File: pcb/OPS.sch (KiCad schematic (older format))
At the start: 36 parts, among them Q13 Q_PNP_EBC, Q14 Q_NPN_ECB, Q15 Q_PNP_EBC, Q16 Q_NPN_ECB, Q17 Q_NPN_ECB, Q18 Q_PNP_EBC, Q19 Q_NPN_ECB, Q20 Q_PNP_EBC, Q21 Q_NPN_ECB, Q22 Q_PNP_EBC, Q23 Q_NPN_ECB, Q24 Q_NPN_ECB, Q25 Q_PNP_EBC, Q26 Q_PNP_EBC

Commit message: Problema sobre power conections arreglado, ahora hay otros quilombos, creo que tiene que ver con el encapsulado de los transistores.
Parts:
- C5, C6: footprint Capacitors_SMD:C_0201 -> Capacitors_SMD:C_0603_HandSoldering
- Q13, Q14, Q15, Q16, Q17, Q18, Q19, Q20, Q21, Q22: footprint Transistors_TO-220:TO-220_Bipolar-BCE_Horizontal -> Transistors_TO-220:TO-220_Bipolar-BCE_Vertical_LargePads
- R15, R16, R17, R18, R19, R20, R21, R22, R23, R24, R25, R26, R27: footprint Resistors_SMD:R_0201 -> Resistors_SMD:R_0603_HandSoldering
- R28: footprint Resistors_SMD:R_0201 -> Resistors_SMD:R_0805_HandSoldering
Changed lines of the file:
@@
 F 0 "Q13" H 3600 1400 50  0000 R CNN
 F 1 "Q_PNP_EBC" H 3900 1300 50  0000 R CNN
-F 2 "Transistors_TO-220:TO-220_Bipolar-BCE_Horizontal" H 3500 1450 29  0001 C CNN
+F 2 "Transistors_TO-220:TO-220_Bipolar-BCE_Vertical_LargePads" H 3500 1450 29  0001 C CNN
 F 3 "" H 3300 1350 60  0000 C CNN
 	1    3300 1350
@@
 F 0 "Q15" H 4200 1400 50  0000 R CNN
 F 1 "Q_PNP_EBC" H 4500 1300 50  0000 R CNN
-F 2 "Transistors_TO-220:TO-220_Bipolar-BCE_Horizontal" H 4100 1450 29  0001 C CNN
+F 2 "Transistors_TO-220:TO-220_Bipolar-BCE_Vertical_LargePads" H 4100 1450 29  0001 C CNN
 F 3 "" H 3900 1350 60  0000 C CNN
 	1    3900 1350
@@
 F 0 "R15" V 3280 1900 50  0000 C CNN
 F 1 "R" V 3200 1900 50  0000 C CNN
-F 2 "Resistors_SMD:R_0201" V 3130 1900 30  0001 C CNN
+F 2 "Resistors_SMD:R_0603_HandSoldering" V 3130 1900 30  0001 C CNN
 F 3 "" H 3200 1900 30  0000 C CNN
 	1    3200 1900
@@
 F 0 "R17" V 4380 2550 50  0000 C CNN
 F 1 "R" V 4300 2550 50  0000 C CNN
-F 2 "Resistors_SMD:R_0201" V 4230 2550 30  0001 C CNN
+F 2 "Resistors_SMD:R_0603_HandSoldering" V 4230 2550 30  0001 C CNN
 F 3 "" H 4300 2550 30  0000 C CNN
 	1    4300 2550
@@
 F 0 "Q21" H 5550 1900 50  0000 R CNN
 F 1 "Q_NPN_ECB" H 5850 1800 50  0000 R CNN
-F 2 "Transistors_TO-220:TO-220_Bipolar-BCE_Horizontal" H 5450 1950 29  0001 C CNN
+F 2 "Transistors_TO-220:TO-220_Bipolar-BCE_Vertical_LargePads" H 5450 1950 29  0001 C CNN
 F 3 "" H 5250 1850 60  0000 C CNN
 	1    5250 1850
@@
 F 0 "R24" V 5430 2200 50  0000 C CNN
 F 1 "R" V 5350 2200 50  0000 C CNN
-F 2 "Resistors_SMD:R_0201" V 5280 2200 30  0001 C CNN
+F 2 "Resistors_SMD:R_0603_HandSoldering" V 5280 2200 30  0001 C CNN
 F 3 "" H 5350 2200 30  0000 C CNN
 	1    5350 2200
@@
 F 0 "Q17" H 4400 3250 50  0000 R CNN
 F 1 "Q_NPN_ECB" H 4700 3150 50  0000 R CNN
-F 2 "Transistors_TO-220:TO-220_Bipolar-BCE_Horizontal" H 4300 3300 29  0001 C CNN
+F 2 "Transistors_TO-220:TO-220_Bipolar-BCE_Vertical_LargePads" H 4300 3300 29  0001 C CNN
 F 3 "" H 4100 3200 60  0000 C CNN
 	1    4100 3200
@@
 F 0 "R19" V 4530 3000 50  0000 C CNN
 F 1 "R" V 4450 3000 50  0000 C CNN
-F 2 "Resistors_SMD:R_0201" V 4380 3000 30  0001 C CNN
+F 2 "Resistors_SMD:R_0603_HandSoldering" V 4380 3000 30  0001 C CNN
 F 3 "" H 4450 3000 30  0000 C CNN
 	1    4450 3000
@@
 F 0 "C5" H 3675 3000 50  0000 L CNN
 F 1 "C" H 3675 2800 50  0000 L CNN
-F 2 "Capacitors_SMD:C_0201" H 3688 2750 30  0001 C CNN
+F 2 "Capacitors_SMD:C_0603_HandSoldering" H 3688 2750 30  0001 C CNN
 F 3 "" H 3650 2900 60  0000 C CNN
 	1    3650 2900
@@
 F 0 "Q19" H 5150 2600 50  0000 R CNN
 F 1 "Q_NPN_ECB" H 5450 2500 50  0000 R CNN
-F 2 "Transistors_TO-220:TO-220_Bipolar-BCE_Horizontal" H 5050 2650 29  0001 C CNN
+F 2 "Transistors_TO-220:TO-220_Bipolar-BCE_Vertical_LargePads" H 5050 2650 29  0001 C CNN
 F 3 "" H 4850 2550 60  0000 C CNN
 	1    4850 2550
@@
 F 0 "R20" V 4530 3550 50  0000 C CNN
 F 1 "R" V 4450 3550 50  0000 C CNN
-F 2 "Resistors_SMD:R_0201" V 4380 3550 30  0001 C CNN
+F 2 "Resistors_SMD:R_0603_HandSoldering" V 4380 3550 30  0001 C CNN
 F 3 "" H 4450 3550 30  0000 C CNN
 	1    4450 3550
@@
 F 0 "R22" V 5030 3250 50  0000 C CNN
 F 1 "R" V 4950 3250 50  0000 C CNN
-F 2 "Resistors_SMD:R_0201" V 4880 3250 30  0001 C CNN
+F 2 "Resistors_SMD:R_0603_HandSoldering" V 4880 3250 30  0001 C CNN
 F 3 "" H 4950 3250 30  0000 C CNN
 	1    4950 3250
@@
 F 0 "R26" V 6030 3300 50  0000 C CNN
 F 1 "R" V 5950 3300 50  0000 C CNN
-F 2 "Resistors_SMD:R_0201" V 5880 3300 30  0001 C CNN
+F 2 "Resistors_SMD:R_0603_HandSoldering" V 5880 3300 30  0001 C CNN
 F 3 "" H 5950 3300 30  0000 C CNN
 	1    5950 3300
@@
 F 0 "R16" V 3280 5200 50  0000 C CNN
 F 1 "R" V 3200 5200 50  0000 C CNN
-F 2 "Resistors_SMD:R_0201" V 3130 5200 30  0001 C CNN
+F 2 "Resistors_SMD:R_0603_HandSoldering" V 3130 5200 30  0001 C CNN
 F 3 "" H 3200 5200 30  0000 C CNN
 	1    3200 5200
@@
 F 0 "R18" V 4380 4550 50  0000 C CNN
 F 1 "R" V 4300 4550 50  0000 C CNN
-F 2 "Resistors_SMD:R_0201" V 4230 4550 30  0001 C CNN
+F 2 "Resistors_SMD:R_0603_HandSoldering" V 4230 4550 30  0001 C CNN
 F 3 "" H 4300 4550 30  0000 C CNN
 	1    4300 4550
@@
 F 0 "R25" V 5430 4900 50  0000 C CNN
 F 1 "R" V 5350 4900 50  0000 C CNN
-F 2 "Resistors_SMD:R_0201" V 5280 4900 30  0001 C CNN
+F 2 "Resistors_SMD:R_0603_HandSoldering" V 5280 4900 30  0001 C CNN
 F 3 "" H 5350 4900 30  0000 C CNN
 	1    5350 4900
@@
 F 0 "R21" V 4530 4100 50  0000 C CNN
 F 1 "R" V 4450 4100 50  0000 C CNN
-F 2 "Resistors_SMD:R_0201" V 4380 4100 30  0001 C CNN
+F 2 "Resistors_SMD:R_0603_HandSoldering" V 4380 4100 30  0001 C CNN
 F 3 "" H 4450 4100 30  0000 C CNN
 	1    4450 4100
@@
 F 0 "C6" H 3675 4300 50  0000 L CNN
 F 1 "C" H 3675 4100 50  0000 L CNN
-F 2 "Capacitors_SMD:C_0201" H 3688 4050 30  0001 C CNN
+F 2 "Capacitors_SMD:C_0603_HandSoldering" H 3688 4050 30  0001 C CNN
 F 3 "" H 3650 4200 60  0000 C CNN
 	1    3650 4200
@@
 F 0 "R23" V 5030 3850 50  0000 C CNN
 F 1 "R" V 4950 3850 50  0000 C CNN
-F 2 "Resistors_SMD:R_0201" V 4880 3850 30  0001 C CNN
+F 2 "Resistors_SMD:R_0603_HandSoldering" V 4880 3850 30  0001 C CNN
 F 3 "" H 4950 3850 30  0000 C CNN
 	1    4950 3850
@@
 F 0 "R27" V 6030 3800 50  0000 C CNN
 F 1 "R" V 5950 3800 50  0000 C CNN
-F 2 "Resistors_SMD:R_0201" V 5880 3800 30  0001 C CNN
+F 2 "Resistors_SMD:R_0603_HandSoldering" V 5880 3800 30  0001 C CNN
 F 3 "" H 5950 3800 30  0000 C CNN
 	1    5950 3800
@@
 F 0 "Q14" H 3600 5800 50  0000 R CNN
 F 1 "Q_NPN_ECB" H 3900 5700 50  0000 R CNN
-F 2 "Transistors_TO-220:TO-220_Bipolar-BCE_Horizontal" H 3500 5850 29  0001 C CNN
+F 2 "Transistors_TO-220:TO-220_Bipolar-BCE_Vertical_LargePads" H 3500 5850 29  0001 C CNN
 F 3 "" H 3300 5750 60  0000 C CNN
 	1    3300 5750
@@
 F 0 "Q18" H 4400 3950 50  0000 R CNN
 F 1 "Q_PNP_EBC" H 4700 3850 50  0000 R CNN
-F 2 "Transistors_TO-220:TO-220_Bipolar-BCE_Horizontal" H 4300 4000 29  0001 C CNN
+F 2 "Transistors_TO-220:TO-220_Bipolar-BCE_Vertical_LargePads" H 4300 4000 29  0001 C CNN
 F 3 "" H 4100 3900 60  0000 C CNN
 	1    4100 3900
@@
 F 0 "Q16" H 4200 5800 50  0000 R CNN
 F 1 "Q_NPN_ECB" H 4500 5700 50  0000 R CNN
-F 2 "Transistors_TO-220:TO-220_Bipolar-BCE_Horizontal" H 4100 5850 29  0001 C CNN
+F 2 "Transistors_TO-220:TO-220_Bipolar-BCE_Vertical_LargePads" H 4100 5850 29  0001 C CNN
 F 3 "" H 3900 5750 60  0000 C CNN
 	1    3900 5750
@@
 F 0 "Q20" H 5150 4600 50  0000 R CNN
 F 1 "Q_PNP_EBC" H 5450 4500 50  0000 R CNN
-F 2 "Transistors_TO-220:TO-220_Bipolar-BCE_Horizontal" H 5050 4650 29  0001 C CNN
+F 2 "Transistors_TO-220:TO-220_Bipolar-BCE_Vertical_LargePads" H 5050 4650 29  0001 C CNN
 F 3 "" H 4850 4550 60  0000 C CNN
 	1    4850 4550
@@
 F 0 "Q22" H 5550 5300 50  0000 R CNN
 F 1 "Q_PNP_EBC" H 5850 5200 50  0000 R CNN
-F 2 "Transistors_TO-220:TO-220_Bipolar-BCE_Horizontal" H 5450 5350 29  0001 C CNN
+F 2 "Transistors_TO-220:TO-220_Bipolar-BCE_Vertical_LargePads" H 5450 5350 29  0001 C CNN
 F 3 "" H 5250 5250 60  0000 C CNN
 	1    5250 5250
@@
 F 0 "R28" V 6480 3800 50  0000 C CNN
 F 1 "R" V 6400 3800 50  0000 C CNN
-F 2 "Resistors_SMD:R_0201" V 6330 3800 30  0001 C CNN
+F 2 "Resistors_SMD:R_0805_HandSoldering" V 6330 3800 30  0001 C CNN
 F 3 "" H 6400 3800 30  0000 C CNN
 	1    6400 3800
@@
 	6400 3550 6400 3650
 $Comp
-L GND #PWR017
+L GND #PWR028
 U 1 1 555E69E7
 P 6400 4000
-F 0 "#PWR017" H 6400 3750 50  0001 C CNN
+F 0 "#PWR028" H 6400 3750 50  0001 C CNN
 F 1 "GND" H 6400 3850 50  0000 C CNN
 F 2 "" H 6400 4000 60  0000 C CNN
@@
 	6400 3950 6400 4000
 $Comp
-L GND #PWR018
+L GND #PWR029
 U 1 1 555F209B
 P 3200 5050
-F 0 "#PWR018" H 3200 4800 50  0001 C CNN
+F 0 "#PWR029" H 3200 4800 50  0001 C CNN
 F 1 "GND" H 3200 4900 50  0000 C CNN
 F 2 "" H 3200 5050 60  0000 C CNN
@@
 $EndComp
 $Comp
-L GND #PWR019
+L GND #PWR030
 U 1 1 555E698A
 P 3200 2100
-F 0 "#PWR019" H 3200 1850 50  0001 C CNN
+F 0 "#PWR030" H 3200 1850 50  0001 C CNN
 F 1 "GND" H 3200 1950 50  0000 C CNN
 F 2 "" H 3200 2100 60  0000 C CNN
@@
 $EndComp
 $Comp
-L +VA #PWR020
+L +VA #PWR031
 U 1 1 555F2B00
 P 6300 900
-F 0 "#PWR020" H 6300 750 50  0001 C CNN
+F 0 "#PWR031" H 6300 750 50  0001 C CNN
 F 1 "+VA" H 6300 1050 50  0000 C CNN
 F 2 "" H 6300 900 60  0000 C CNN
@@
 $EndComp
 $Comp
-L +VB #PWR021
+L +VB #PWR032
 U 1 1 555F2D0C
 P 6450 2500
-F 0 "#PWR021" H 6450 2350 50  0001 C CNN
+F 0 "#PWR032" H 6450 2350 50  0001 C CNN
 F 1 "+VB" H 6450 2650 50  0000 C CNN
 F 2 "" H 6450 2500 60  0000 C CNN
@@
 $EndComp
 $Comp
-L -VB #PWR022
+L -VB #PWR033
 U 1 1 555F3146
 P 6450 4600
-F 0 "#PWR022" H 6450 4450 50  0001 C CNN
+F 0 "#PWR033" H 6450 4450 50  0001 C CNN
 F 1 "-VB" H 6450 4750 50  0000 C CNN
 F 2 "" H 6450 4600 60  0000 C CNN
@@
 $EndComp
 $Comp
-L -VA #PWR023
+L -VA #PWR034
 U 1 1 555F3328
 P 6300 6200
-F 0 "#PWR023" H 6300 6050 50  0001 C CNN
+F 0 "#PWR034" H 6300 6050 50  0001 C CNN
 F 1 "-VA" H 6300 6350 50  0000 C CNN
 F 2 "" H 6300 6200 60  0000 C CNN

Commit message: Sigo trabajando en el PCB usando Kicad, necesito mas info sobre los diodos para continuar.
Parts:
- removed Q14, Q16, Q19: Q_NPN_ECB, Transistors_TO-220:TO-220_Bipolar-BCE_Vertical_LargePads, symbol Q_NPN_ECB
- removed Q18: Q_PNP_EBC, Transistors_TO-220:TO-220_Bipolar-BCE_Vertical_LargePads, symbol Q_PNP_EBC
- removed Q23, Q24: Q_NPN_ECB, Transistors_TO-220:TO-220_Bipolar-BCE_Horizontal, symbol Q_NPN_ECB
- removed Q25, Q26: Q_PNP_EBC, Transistors_TO-220:TO-220_Bipolar-BCE_Horizontal, symbol Q_PNP_EBC
- added P10, P11: 2SC3281, Pin_Headers:Pin_Header_Straight_1x03, symbol CONN_01X03
- added P12, P9: 2SA1302, Pin_Headers:Pin_Header_Straight_1x03, symbol CONN_01X03
- added P7: MJE350, Pin_Headers:Pin_Header_Straight_1x03, symbol CONN_01X03
- added P8: MJE340, Pin_Headers:Pin_Header_Straight_1x03, symbol CONN_01X03
- added Q14, Q16: MPSA06_NPN_EBC, Transistors_TO-220:TO-220_Bipolar-BCE_Vertical_LargePads, symbol Q_NPN_EBC
- Q13, Q15: value Q_PNP_EBC -> MPSA56_PNP_EBC
- Q17: value Q_NPN_ECB -> MJE340_NPN_ECB
- Q18: renamed from Q20; value Q_PNP_EBC -> MJE350_PNP_EBC
- Q19: renamed from Q21; value Q_NPN_ECB -> MJE340_NPN_ECB
- Q20: renamed from Q22; value Q_PNP_EBC -> MJE350_PNP_EBC
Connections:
- net +VA: now also Q17.2 (C), P11.2 (P2)
- net -VA: now also P12.3 (P3), Q14.1 (E), Q16.1 (E)
- net TO_OPS: now also P7.1 (P1), P8.1 (P1); no longer Q17.1 (E)
- net at C5.1, D1.2 (K), R17.2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: now also P7.2 (P2); no longer Q17.2 (C)
- net at R17.1: now also Q17.3 (B)
- net at Q19.1 (E), R24.2: now also P11.1 (P1)
- net at D5.1 (A), R24.1: now also P10.2 (P2), P11.3 (P3)
- net at R19.1, R20.2: now also P7.3 (P3); no longer Q17.3 (B)
- net at R22.2: now also Q17.1 (E), P10.1 (P1)
- net at R20.1, R21.1: now also P8.3 (P3)
- net at R26.2: now also P10.3 (P3)
- net at R16.1: now also Q14.2 (B), Q14.3 (C), Q16.2 (B)
- net at D2.2 (K), D4.1 (A): now also Q16.3 (C)
- net at C6.1, D2.1 (A), R18.2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: now also P8.2 (P2)
- net at D6.2 (K), R25.1: now also P12.2 (P2), P9.2 (P2)
- net at Q20.1 (E), R25.2: now also P12.1 (P1)
- net at Q18.1 (E), R23.2: now also P9.1 (P1)
- net at R27.2: now also P9.3 (P3)
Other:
- note added: "Acoplación\nTérmica\n"
- note added: "B"
- note added: "C"
- note added: "E"

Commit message: Agrego algunos datasheets, el export kicad en pdf y sigo trabajando en el PCB
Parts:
- removed C6: C, Capacitors_SMD:C_0603_HandSoldering, symbol C
- removed D1: D_Schottky, Diodes_ThroughHole:Diode_DO-35_SOD27_Horizontal_RM10, symbol D_Schottky
- removed R20: R, Resistors_SMD:R_0603_HandSoldering, symbol R
- added C10, C11, C12, C13, C14, C15: C, Capacitors_Elko_ThroughHole:Elko_vert_11.5x8mm_RM3.5, symbol C
- added D1: ZENER, symbol ZENER
- added L1: INDUCTOR, symbol INDUCTOR
- added R21, R30, R31: R, Resistors_SMD:R_0603_HandSoldering, symbol R
- added RV2: POT, symbol POT
- C9: renamed from C5; footprint Capacitors_SMD:C_0603_HandSoldering -> Capacitors_Elko_ThroughHole:Elko_vert_11.5x8mm_RM3.5
- Q13, Q14, Q15, Q16, Q17, Q18, Q19, Q20: footprint Transistors_TO-220:TO-220_Bipolar-BCE_Vertical_LargePads -> Transistors_TO-220:TO-220_Neutral123_Vertical
- renumbered D6 to D5, D5 to D6, P11 to P10, P12 to P11, P7 to P6, P8 to P7, P9 to P8, P10 to P9, R15 to R16, R16 to R17, R17 to R18, R18 to R19, R19 to R20, R21 to R22, R22 to R23, R23 to R24, R24 to R25, R25 to R26, R26 to R27, R27 to R28, R28 to R29
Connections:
- net +VB: now also C13.1
- net -VA: now also P11.2 (P2); no longer P11.3 (P3)
- net GND: now also C11.2, C12.2, C13.2, C14.2
- net OUT: now also L1.1, R31.1; no longer R27.1, R28.1, R29.1
- net TO_OPS: no longer C9.2
- net at D3.2 (K), Q15.3 (C): now also D1.1 (A)
- net at C9.1, P6.2 (P2), R18.2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: now also D1.2 (K)
- net at P6.3 (P3), R20.1: now also RV2.1
- net at P7.3 (P3), R22.1: now also R21.2
- net at R23.1: now also C10.1; no longer R24.1
- net at D2.1 (A), P7.2 (P2), R19.2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: now also C9.2
- net at D5.2 (K), P8.2 (P2), R26.1: now also P11.3 (P3); no longer P11.2 (P2)
- new net: C10.2, R24.1
- new net: R21.1, RV2.2, RV2.3
- new net: C15.1, R30.2
- new net FBACK: L1.2, R27.1, R28.1, R29.1, R30.1, R31.2
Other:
- note added: "Red Zobel\n"
- moved on the sheet: D6, R20, R22

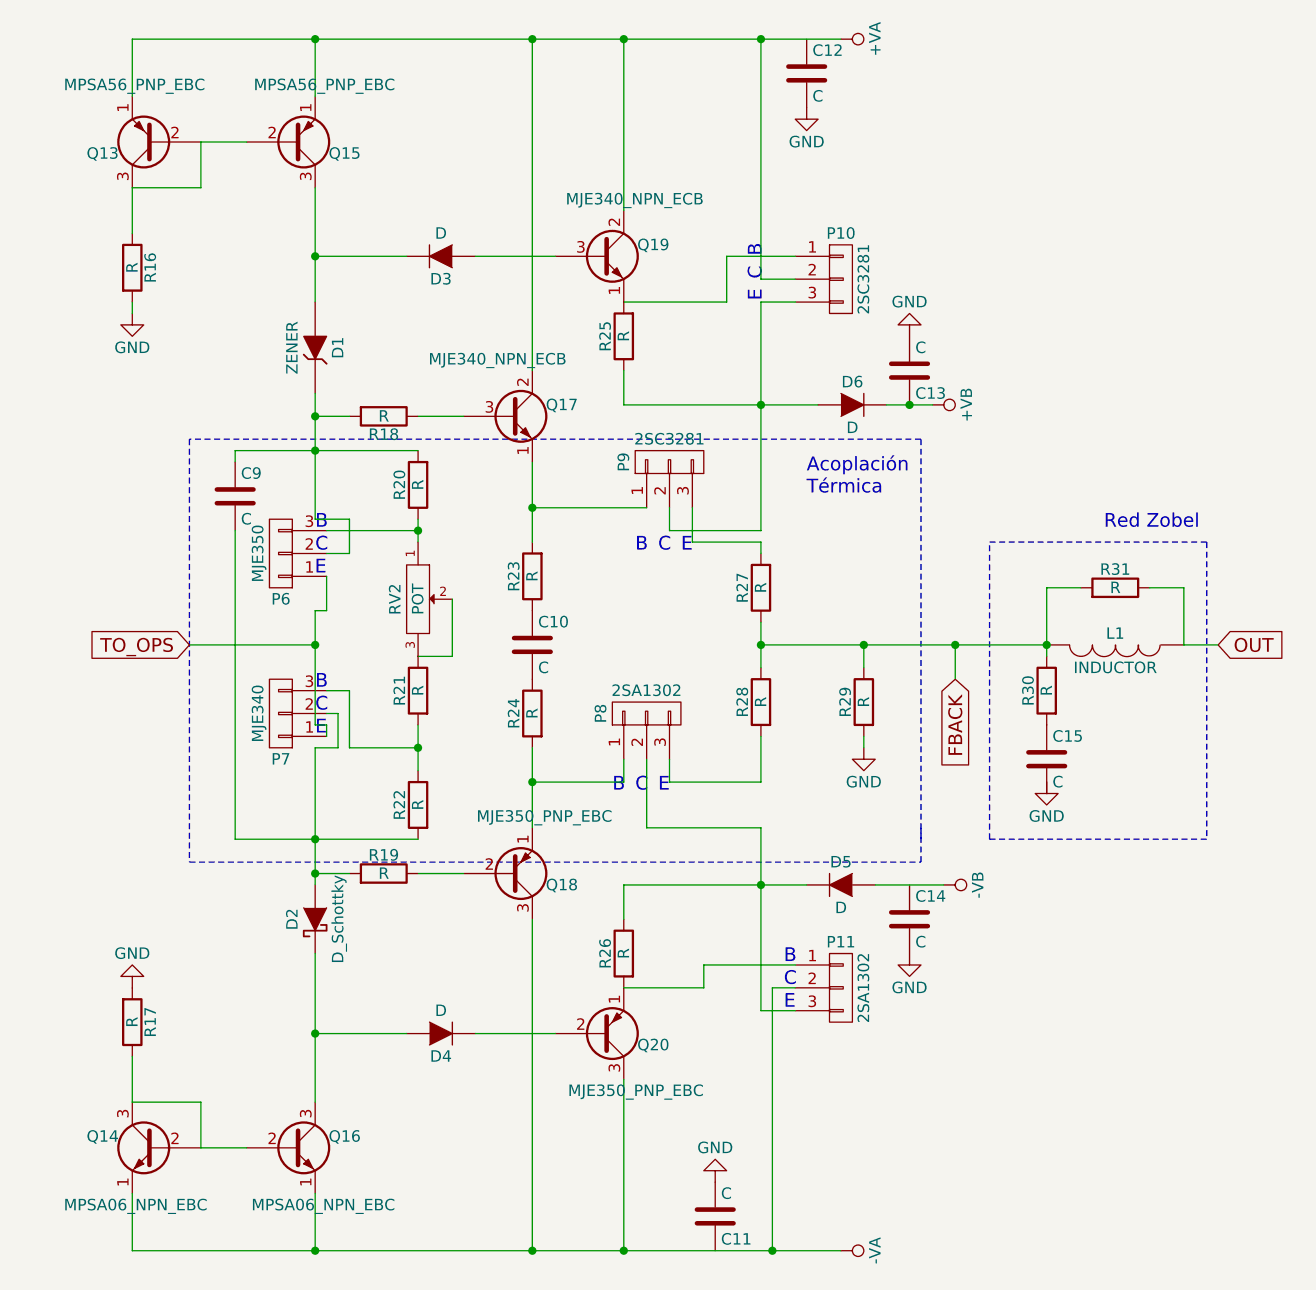
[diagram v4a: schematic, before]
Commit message: Termino la primera version del PCB para el amplificador, queda engordar las pistas que llevan alta corriente.
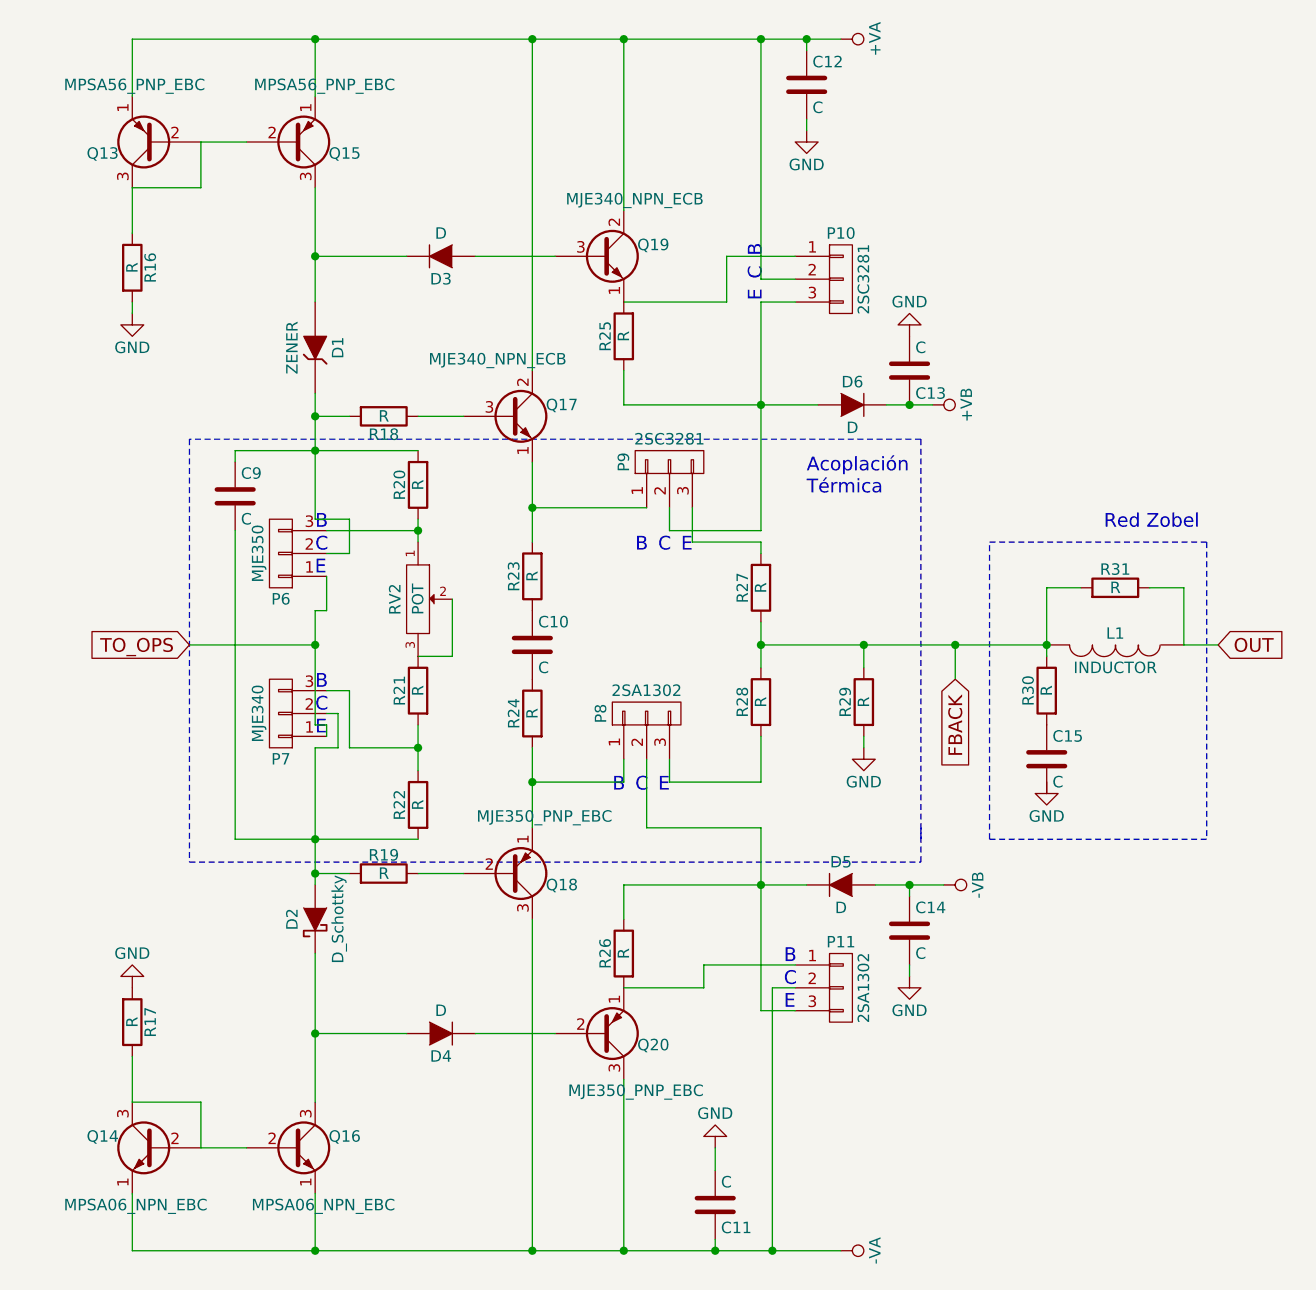
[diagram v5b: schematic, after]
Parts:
- D1: footprint (none) -> Diodes_ThroughHole:Diode_DO-35_SOD27_Horizontal_RM10
- L1: footprint (none) -> Resistors_ThroughHole:Resistor_Horizontal_RM10mm
- R16, R17, R18, R19, R20, R21, R22, R23, R24, R25, R26, R27, R28, R30, R31: footprint Resistors_SMD:R_0603_HandSoldering -> Resistors_ThroughHole:Resistor_Horizontal_RM10mm
- R29: footprint Resistors_SMD:R_0805_HandSoldering -> Resistors_ThroughHole:Resistor_Horizontal_RM10mm
- RV2: footprint (none) -> Pin_Headers:Pin_Header_Straight_1x03
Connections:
- net +VA: now also C12.1
- net -VA: now also C11.1
- net -VB: now also C14.1
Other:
- moved on the sheet: C11, C12, C14

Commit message: Arreglo problema, se mostraba cobre en el front , solo lo hice para Q1, queda hacerlo en todos y ajustar bien los drills, acorde a los que existen en el LCI...
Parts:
- R27, R28: footprint Resistors_ThroughHole:Resistor_Horizontal_RM10mm -> Resistors_ThroughHole:Resistor_Ceramic_Horizontal_L23mm-W9mm-H9mm-p30mm
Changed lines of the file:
@@
 EESchema Schematic File Version 2
+LIBS:lib_ampli
 LIBS:power
 LIBS:device
@@
 F 0 "R27" V 6030 3300 50  0000 C CNN
 F 1 "R" V 5950 3300 50  0000 C CNN
-F 2 "Resistors_ThroughHole:Resistor_Horizontal_RM10mm" V 5880 3300 30  0001 C CNN
+F 2 "Resistors_ThroughHole:Resistor_Ceramic_Horizontal_L23mm-W9mm-H9mm-p30mm" V 5880 3300 30  0001 C CNN
 F 3 "" H 5950 3300 30  0000 C CNN
 	1    5950 3300
@@
 F 0 "R28" V 6030 3800 50  0000 C CNN
 F 1 "R" V 5950 3800 50  0000 C CNN
-F 2 "Resistors_ThroughHole:Resistor_Horizontal_RM10mm" V 5880 3800 30  0001 C CNN
+F 2 "Resistors_ThroughHole:Resistor_Ceramic_Horizontal_L23mm-W9mm-H9mm-p30mm" V 5880 3800 30  0001 C CNN
 F 3 "" H 5950 3800 30  0000 C CNN
 	1    5950 3800
@@
 	4000 2450 4000 3000
 Wire Wire Line
-	4050 3150 4150 3150
+	4150 3150 4050 3150
 Wire Wire Line
 	4050 3400 4050 3250
@@
 	5350 4750 5350 4600
 Wire Wire Line
-	5350 5050 5700 5050
+	5700 5050 5350 5050
 Wire Wire Line
 	4700 5250 5050 5250
